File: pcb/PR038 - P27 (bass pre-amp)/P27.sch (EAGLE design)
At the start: 52 parts, among them IC1 NE5532U, IC2 LM317, T1 BC847

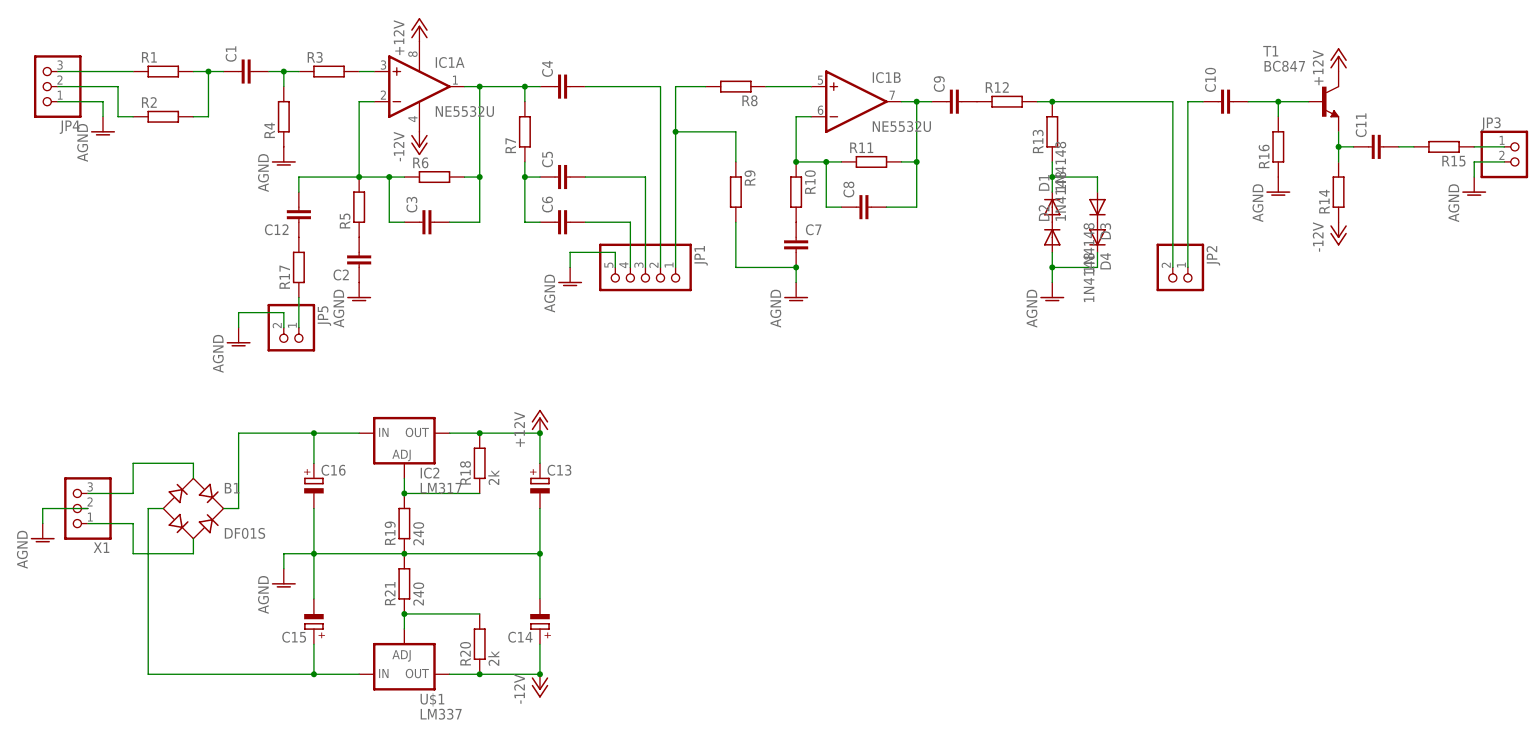
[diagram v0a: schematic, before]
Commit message: 
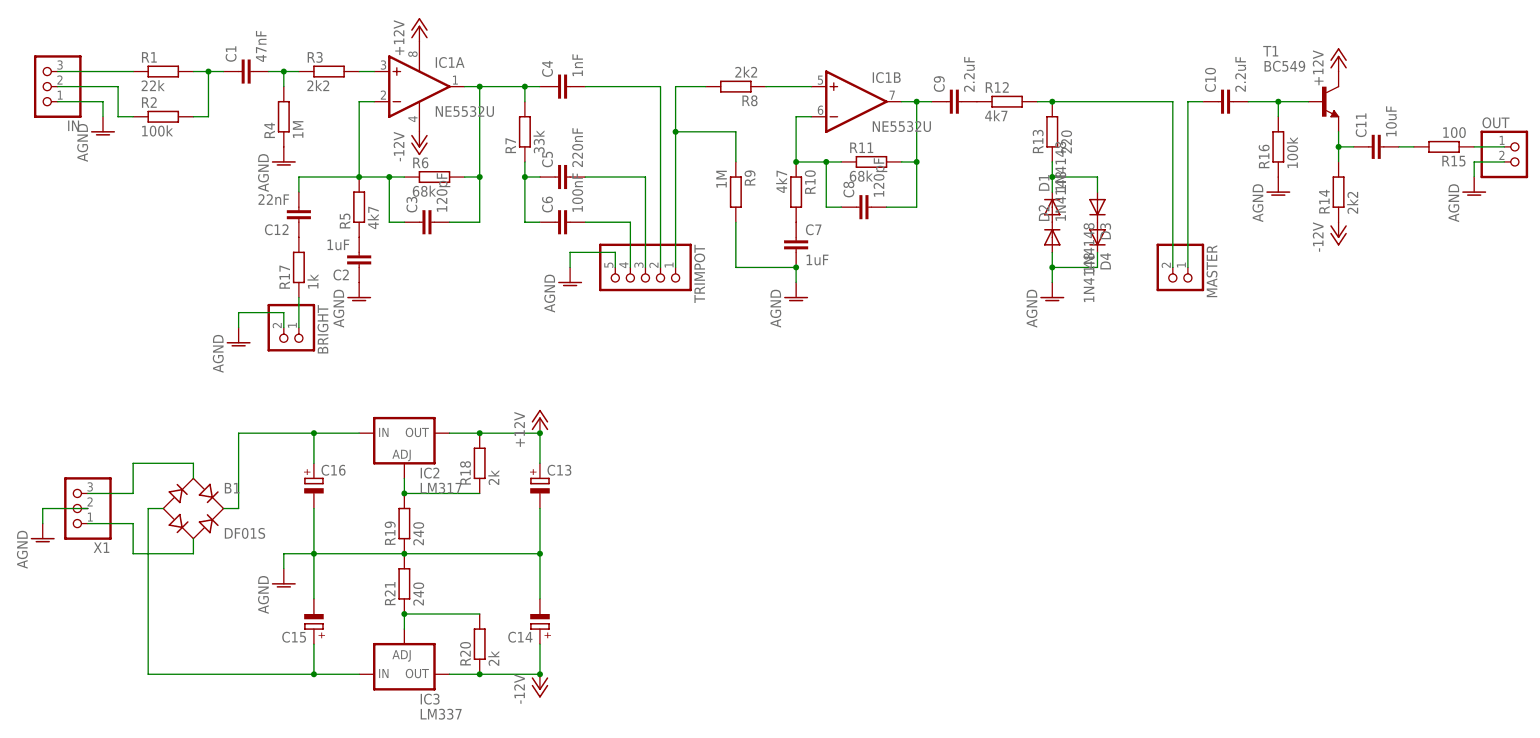
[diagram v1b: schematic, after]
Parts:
- C1: value (none) -> 47nF
- C10, C9: value (none) -> 2.2uF; device P27:C-EUC0805K -> P27:C-EUC1206
- C11: value (none) -> 10uF; device P27:C-EUC0805K -> P27:C-EUC1206
- C12: value (none) -> 22nF
- C2, C7: value (none) -> 1uF
- C3, C8: value (none) -> 120pF
- C4: value (none) -> 1nF
- C5: value (none) -> 220nF
- C6: value (none) -> 100nF
- R1: value (none) -> 22k
- R10, R12, R5: value (none) -> 4k7
- R11, R6: value (none) -> 68k
- R13: value (none) -> 220
- R14, R3, R8: value (none) -> 2k2
- R15: value (none) -> 100
- R16, R2: value (none) -> 100k
- R17: value (none) -> 1k
- R4, R9: value (none) -> 1M
- R7: value (none) -> 33k
- T1: value BC847 -> BC549
- renumbered JP1 to TRIMPOT, JP2 to MASTER, JP3 to OUT, JP4 to IN, JP5 to BRIGHT, U$1 to IC3
